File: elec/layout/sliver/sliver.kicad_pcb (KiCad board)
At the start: 2 copper layers, 64 x 4 mm, 6 parts

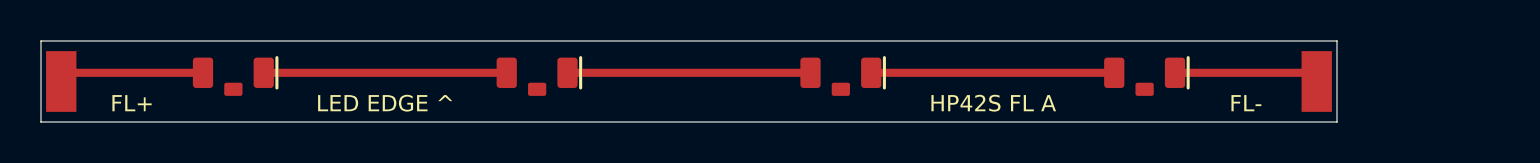
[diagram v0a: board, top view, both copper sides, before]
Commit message: mip: LS032 circuit, 155 mm board, six-LED sliver
display.ato: the e-paper booster is replaced by a TPS610997 5 V boost
(VDD and VDDA together, as Sharp allows), J2 is the Hirose FH34SRJ-10S with
panel pin n on connector pin n, and an RV-8263-C7 on the I2C bus supplies
EXTCOMIN from CLKOUT, gated by CLKOE on IO36. Footprints for the three from
the Hirose catalogue, TI YFF0006 drawing and Micro Crystal datasheet.

Board: variant.py DROP = 11, BOARD_H = 155, glass Y 12..59.02; the board
file stretched once by mip_drop_board.py, FPC notch re-centred on the new
tail, stale zone fills dropped. Placement table re-keyed for the renumbered
designators with the new display block; route_power loses the e-paper
booster's routes. Sliver is 72 mm with six LEDs.

The netlist still has to be imported in KiCad before placement and routing.

Co-Authored-By: Claude Opus 5.5 (1M context) <noreply@anthropic.com>
Claude-Session: https://claude.ai/code/session_01Fsrot3PauY1JdFC7HgzJ33
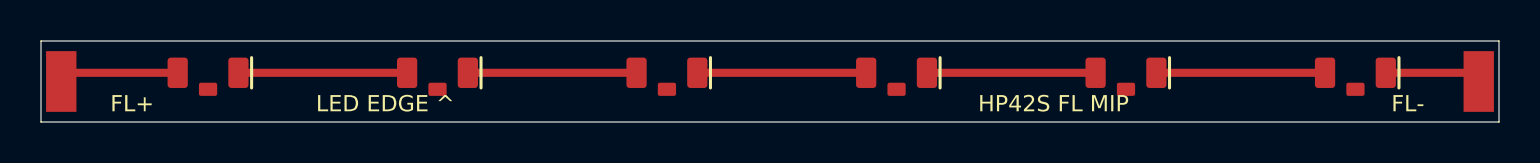
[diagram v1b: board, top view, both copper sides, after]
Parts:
- added D5: 599-2Q01-147F, hp42s:Dialight_599_White_1208_RA, F.Cu at (53.6, 1.57)
- added D6: 599-2Q01-147F, hp42s:Dialight_599_White_1208_RA, F.Cu at (64.9, 1.57)
- moved D4 12.2 mm to (42.2, 1.57)
- moved D3 8.59 mm to (30.9, 1.57)
- moved TP2 8.00 mm to (71.0, 2.00)
- moved D2 4.92 mm to (19.6, 1.57)
- moved D1 1.25 mm to (8.25, 1.57)
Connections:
- D4 pad 1: fb -> n4
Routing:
- net n5: track 0.00 -> 8.33 mm
- net n4: track 0.00 -> 8.33 mm
- net n1: track 12.0 -> 8.33 mm
- net n2: track 12.0 -> 8.33 mm
- net n3: track 12.0 -> 8.34 mm
- net fb: track 7.00 -> 4.59 mm
- net vled: track 7.00 -> 5.75 mm
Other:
- board size 64 x 4 mm -> 72 x 4 mm
- board text added: "HP42S FL MIP"
- board text removed: "HP42S FL A"
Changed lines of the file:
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@@
 	(footprint "hp42s:Dialight_599_White_1208_RA"
 		(layer "F.Cu")
-		(at 9.5 1.57)
+		(at 8.25 1.57)
 		(descr "Dialight 599 series MicroLED, single-colour 1208 right angle. Pad 2 anode, pad 1 cathode, pad 3 mechanical. Lens faces -y.")
 		(property "Reference" "D1"
@@
 	(footprint "hp42s:Dialight_599_White_1208_RA"
 		(layer "F.Cu")
-		(at 24.5 1.57)
+		(at 19.58 1.57)
 		(descr "Dialight 599 series MicroLED, single-colour 1208 right angle. Pad 2 anode, pad 1 cathode, pad 3 mechanical. Lens faces -y.")
 		(property "Reference" "D2"
@@
 	(footprint "hp42s:Dialight_599_White_1208_RA"
 		(layer "F.Cu")
-		(at 39.5 1.57)
+		(at 30.91 1.57)
 		(descr "Dialight 599 series MicroLED, single-colour 1208 right angle. Pad 2 anode, pad 1 cathode, pad 3 mechanical. Lens faces -y.")
 		(property "Reference" "D3"
@@
 	(footprint "hp42s:Dialight_599_White_1208_RA"
 		(layer "F.Cu")
-		(at 54.5 1.57)
+		(at 42.25 1.57)
 		(descr "Dialight 599 series MicroLED, single-colour 1208 right angle. Pad 2 anode, pad 1 cathode, pad 3 mechanical. Lens faces -y.")
 		(property "Reference" "D4"
@@
 			(layers "F.Cu" "F.Paste" "F.Mask")
 			(roundrect_rratio 0.15)
+			(net "n4")
+		)
+		(pad "3" smd roundrect
+			(at 0 0.815)
+			(size 0.9 0.65)
+			(layers "F.Cu" "F.Paste" "F.Mask")
+			(roundrect_rratio 0.15)
+		)
+		(model "${KIPRJMOD}/../../footprints/hp42s.3dshapes/Dialight_599_White_1208_RA.step"
+			(offset (xyz 0 0 0))
+			(scale (xyz 1 1 1))
+			(rotate (xyz 0 0 0))
+		)
+		(embedded_fonts no)
+	)
+	(footprint "hp42s:Dialight_599_White_1208_RA"
+		(layer "F.Cu")
+		(at 53.58 1.57)
+		(descr "Dialight 599 series MicroLED, single-colour 1208 right angle. Pad 2 anode, pad 1 cathode, pad 3 mechanical. Lens faces -y.")
+		(property "Reference" "D5"
+			(at 0 2.3 0)
+			(layer "F.Fab")
+			(effects (font (size 0.8 0.8) (thickness 0.12)))
+		)
+		(property "Value" "599-2Q01-147F"
+			(at 0 3.2 0)
+			(layer "F.Fab")
+			(hide yes)
+			(effects (font (size 0.8 0.8) (thickness 0.12)))
+		)
+		(attr smd)
+		(fp_rect (start -1.5 -0.5) (end 1.5 0.5)
+			(stroke (width 0.1) (type solid))
+			(fill no)
+			(layer "F.Fab")
+		)
+		(fp_rect (start -2.25 -1.82) (end 2.25 1.4)
+			(stroke (width 0.05) (type solid))
+			(fill no)
+			(layer "F.CrtYd")
+		)
+		(fp_line (start 2.15 -0.75) (end 2.15 0.75)
+			(stroke (width 0.15) (type solid))
+			(layer "F.SilkS")
+		)
+		(pad "2" smd roundrect
+			(at -1.5 0)
+			(size 1 1.5)
+			(layers "F.Cu" "F.Paste" "F.Mask")
+			(roundrect_rratio 0.15)
+			(net "n4")
+		)
+		(pad "1" smd roundrect
+			(at 1.5 0)
+			(size 1 1.5)
+			(layers "F.Cu" "F.Paste" "F.Mask")
+			(roundrect_rratio 0.15)
+			(net "n5")
+		)
+		(pad "3" smd roundrect
+			(at 0 0.815)
+			(size 0.9 0.65)
+			(layers "F.Cu" "F.Paste" "F.Mask")
+			(roundrect_rratio 0.15)
+		)
+		(model "${KIPRJMOD}/../../footprints/hp42s.3dshapes/Dialight_599_White_1208_RA.step"
+			(offset (xyz 0 0 0))
+			(scale (xyz 1 1 1))
+			(rotate (xyz 0 0 0))
+		)
+		(embedded_fonts no)
+	)
+	(footprint "hp42s:Dialight_599_White_1208_RA"
+		(layer "F.Cu")
+		(at 64.91 1.57)
+		(descr "Dialight 599 series MicroLED, single-colour 1208 right angle. Pad 2 anode, pad 1 cathode, pad 3 mechanical. Lens faces -y.")
+		(property "Reference" "D6"
+			(at 0 2.3 0)
+			(layer "F.Fab")
+			(effects (font (size 0.8 0.8) (thickness 0.12)))
+		)
+		(property "Value" "599-2Q01-147F"
+			(at 0 3.2 0)
+			(layer "F.Fab")
+			(hide yes)
+			(effects (font (size 0.8 0.8) (thickness 0.12)))
+		)
+		(attr smd)
+		(fp_rect (start -1.5 -0.5) (end 1.5 0.5)
+			(stroke (width 0.1) (type solid))
+			(fill no)
+			(layer "F.Fab")
+		)
+		(fp_rect (start -2.25 -1.82) (end 2.25 1.4)
+			(stroke (width 0.05) (type solid))
+			(fill no)
+			(layer "F.CrtYd")
+		)
+		(fp_line (start 2.15 -0.75) (end 2.15 0.75)
+			(stroke (width 0.15) (type solid))
+			(layer "F.SilkS")
+		)
+		(pad "2" smd roundrect
+			(at -1.5 0)
+			(size 1 1.5)
+			(layers "F.Cu" "F.Paste" "F.Mask")
+			(roundrect_rratio 0.15)
+			(net "n5")
+		)
+		(pad "1" smd roundrect
+			(at 1.5 0)
+			(size 1 1.5)
+			(layers "F.Cu" "F.Paste" "F.Mask")
+			(roundrect_rratio 0.15)
 			(net "fb")
 		)
@@
 	(footprint "hp42s:Frontlight_SliverWirePad"
 		(layer "F.Cu")
-		(at 63 2)
+		(at 71 2)
 		(descr "Where a 30 AWG wire from the main board lands. On the 2 mm of sliver that overhangs the light guide, so the joint is clear of it. Hand soldered: no paste.")
 		(property "Reference" "TP2"
@@
 	(segment
 		(start 1 1.57)
-		(end 8 1.57)
+		(end 6.75 1.57)
 		(width 0.4)
 		(layer "F.Cu")
@@
 	)
 	(segment
-		(start 11 1.57)
-		(end 23 1.57)
+		(start 9.75 1.57)
+		(end 18.08 1.57)
 		(width 0.4)
 		(layer "F.Cu")
@@
 	)
 	(segment
-		(start 26 1.57)
-		(end 38 1.57)
+		(start 21.08 1.57)
+		(end 29.41 1.57)
 		(width 0.4)
 		(layer "F.Cu")
@@
 	)
 	(segment
-		(start 41 1.57)
-		(end 53 1.57)
+		(start 32.41 1.57)
+		(end 40.75 1.57)
 		(width 0.4)
 		(layer "F.Cu")
@@
 	)
 	(segment
-		(start 56 1.57)
-		(end 63 1.57)
+		(start 43.75 1.57)
+		(end 52.08 1.57)
+		(width 0.4)
+		(layer "F.Cu")
+		(net "n4")
+	)
+	(segment
+		(start 55.08 1.57)
+		(end 63.41 1.57)
+		(width 0.4)
+		(layer "F.Cu")
+		(net "n5")
+	)
+	(segment
+		(start 66.41 1.57)
+		(end 71 1.57)
 		(width 0.4)
 		(layer "F.Cu")
@@
 	(gr_line
 		(start 0 0)
-		(end 64 0)
+		(end 72 0)
 		(stroke (width 0.05) (type solid))
 		(layer "Edge.Cuts")
 	)
 	(gr_line
-		(start 64 0)
-		(end 64 4)
+		(start 72 0)
+		(end 72 4)
 		(stroke (width 0.05) (type solid))
 		(layer "Edge.Cuts")
 	)
 	(gr_line
-		(start 64 4)
+		(start 72 4)
 		(end 0 4)
 		(stroke (width 0.05) (type solid))
@@
 	)
 	(gr_text "FL-"
-		(at 59.5 3.1 0)
+		(at 67.5 3.1 0)
 		(layer "F.SilkS")
 		(effects (font (size 0.8 0.8) (thickness 0.12)))
@@
 		(effects (font (size 0.8 0.8) (thickness 0.12)))
 	)
-	(gr_text "HP42S FL A"
-		(at 47 3.1 0)
+	(gr_text "HP42S FL MIP"
+		(at 50 3.1 0)
 		(layer "F.SilkS")
 		(effects (font (size 0.8 0.8) (thickness 0.12)))
